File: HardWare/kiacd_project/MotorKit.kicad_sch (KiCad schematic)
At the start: 35 parts, among them J1 SWD, J2 DBUG, J3 JumpM0, J4 EncM0, J5 JumpM1, J6 EncM1, Q1 8050-Y1, Q2 8050-Y1, U1 STM32F405RGTx, Y1 3225 8M 12PF 10PPM

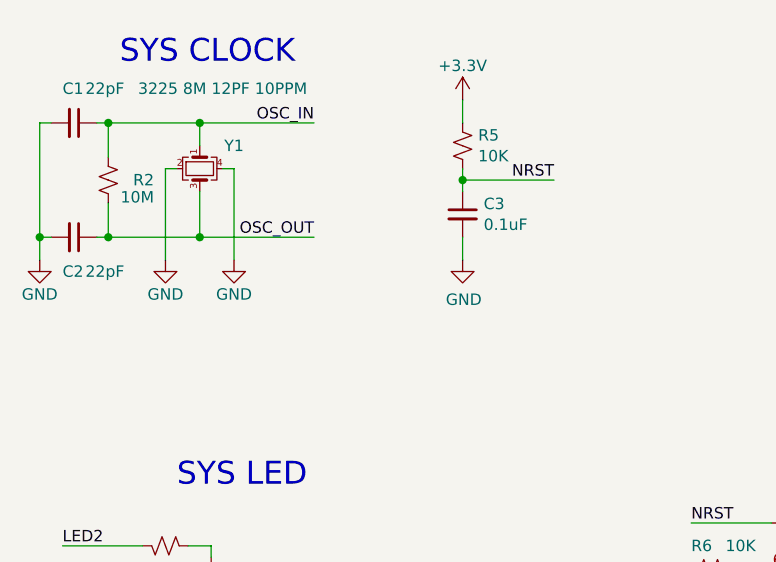
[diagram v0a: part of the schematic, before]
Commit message: 新增工程配置，硬件验证
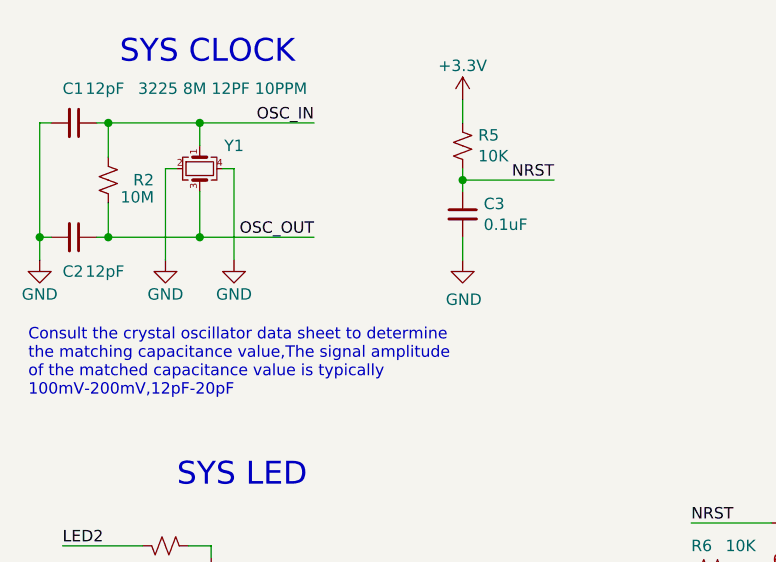
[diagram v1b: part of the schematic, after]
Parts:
- C1, C2: value 22pF -> 12pF
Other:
- note added: "Consult the crystal oscillator data sheet to determine the matching capacitance value,The signal amplitude of the matched capacitance value is typically 100mV-200mV,12pF-20pF"
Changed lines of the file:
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@@
     (effects (font (size 2.54 2.54) bold) (justify left bottom))
+  )
+  (text "Consult the crystal oscillator data sheet to determine \nthe matching capacitance value,The signal amplitude \nof the matched capacitance value is typically \n100mV-200mV,12pF-20pF"
+    (at 20.32 57.15 0)
+    (effects (font (size 1.27 1.27)) (justify left bottom))
   )
   (text "SYS CLOCK" (at 30.48 20.32 0)
@@
       (effects (font (size 1.27 1.27)) (justify left))
     )
-    (property "Value" "22pF" (at 26.67 43.18 90)
+    (property "Value" "12pF" (at 26.67 43.18 90)
       (effects (font (size 1.27 1.27)) (justify left))
     )
@@
       (effects (font (size 1.27 1.27)) (justify left))
     )
-    (property "Value" "22pF" (at 26.67 22.86 90)
-      (effects (font (size 1.27 1.27)) (justify left))
-    )
+    (property "Value" "12pF" (at 26.67 22.86 90)
+      (effects (font (size 1.27 1.27)) (justify left))
+    )
